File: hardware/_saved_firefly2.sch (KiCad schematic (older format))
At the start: 20 parts, among them J1 10118194-0001LF, P2 CONN_01X03, P3 CONN_01X04, P4 CONN_01X05, P5 CONN_01X01, U1 SAM_D11C, U2 RFM69CW, U3 MIC5504

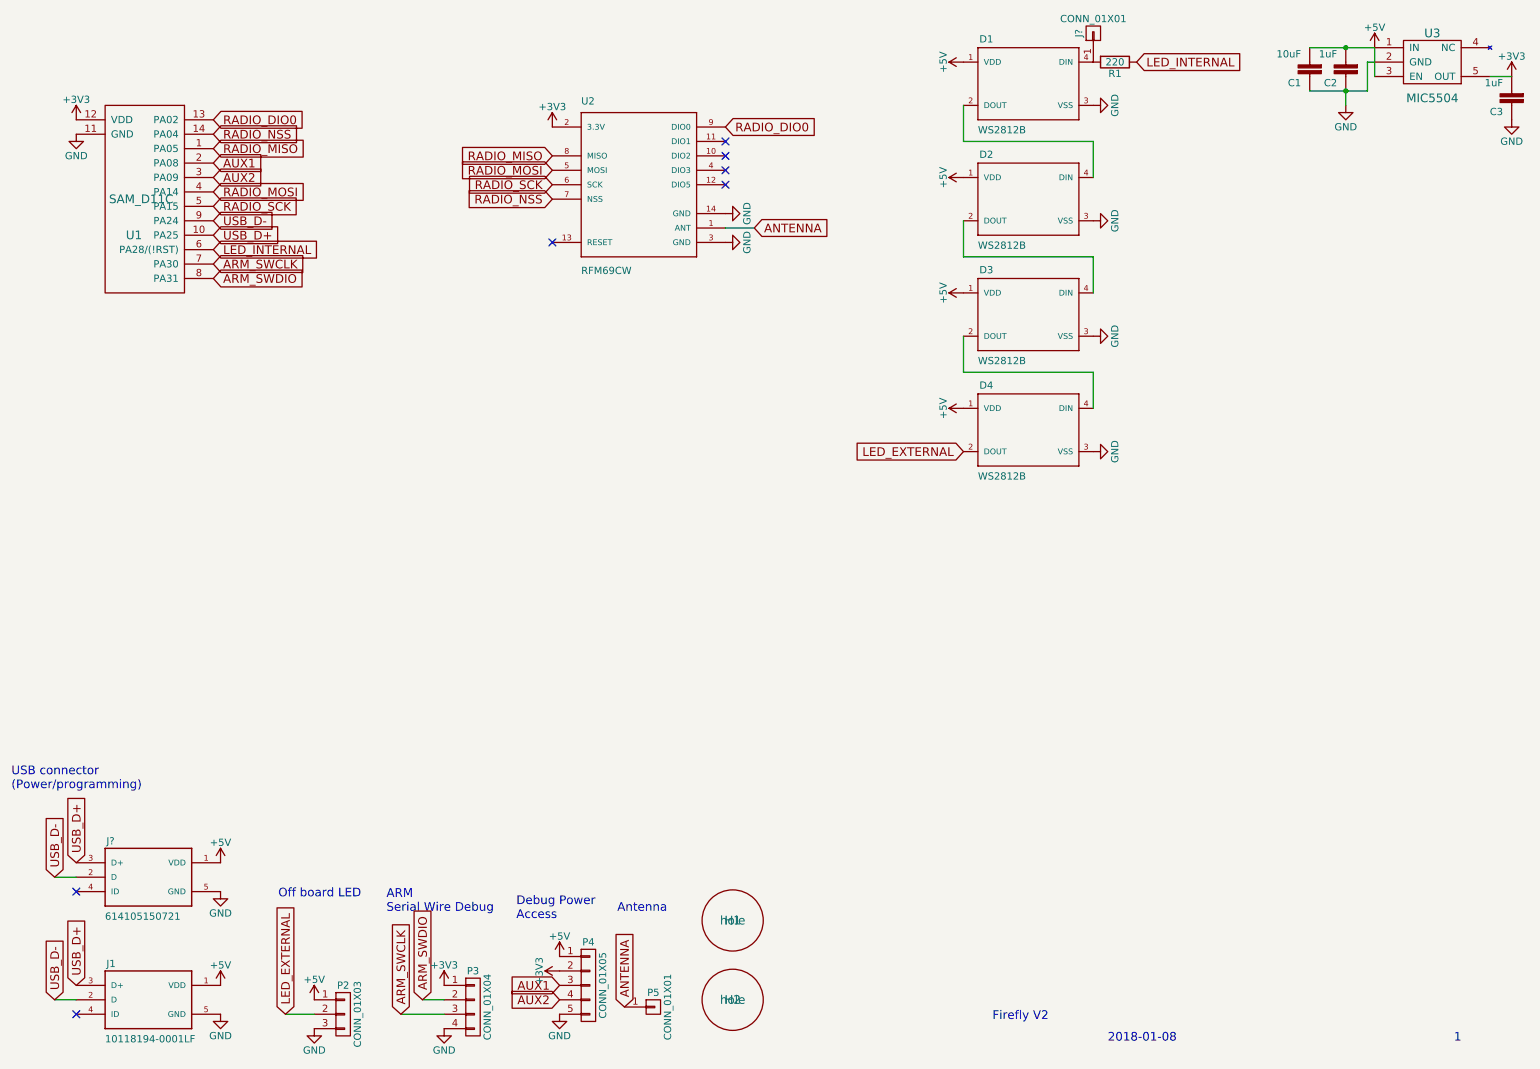
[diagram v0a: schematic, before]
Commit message: Hardware v2.1 Mark orientation for LEDs and radio. Tie enable high on the LDO. Add vertical USB connector and fix horizontal USB connector.
Change-Id: I3b6b9a9fcd473732bc67a64c80cbd03d1b6050b8
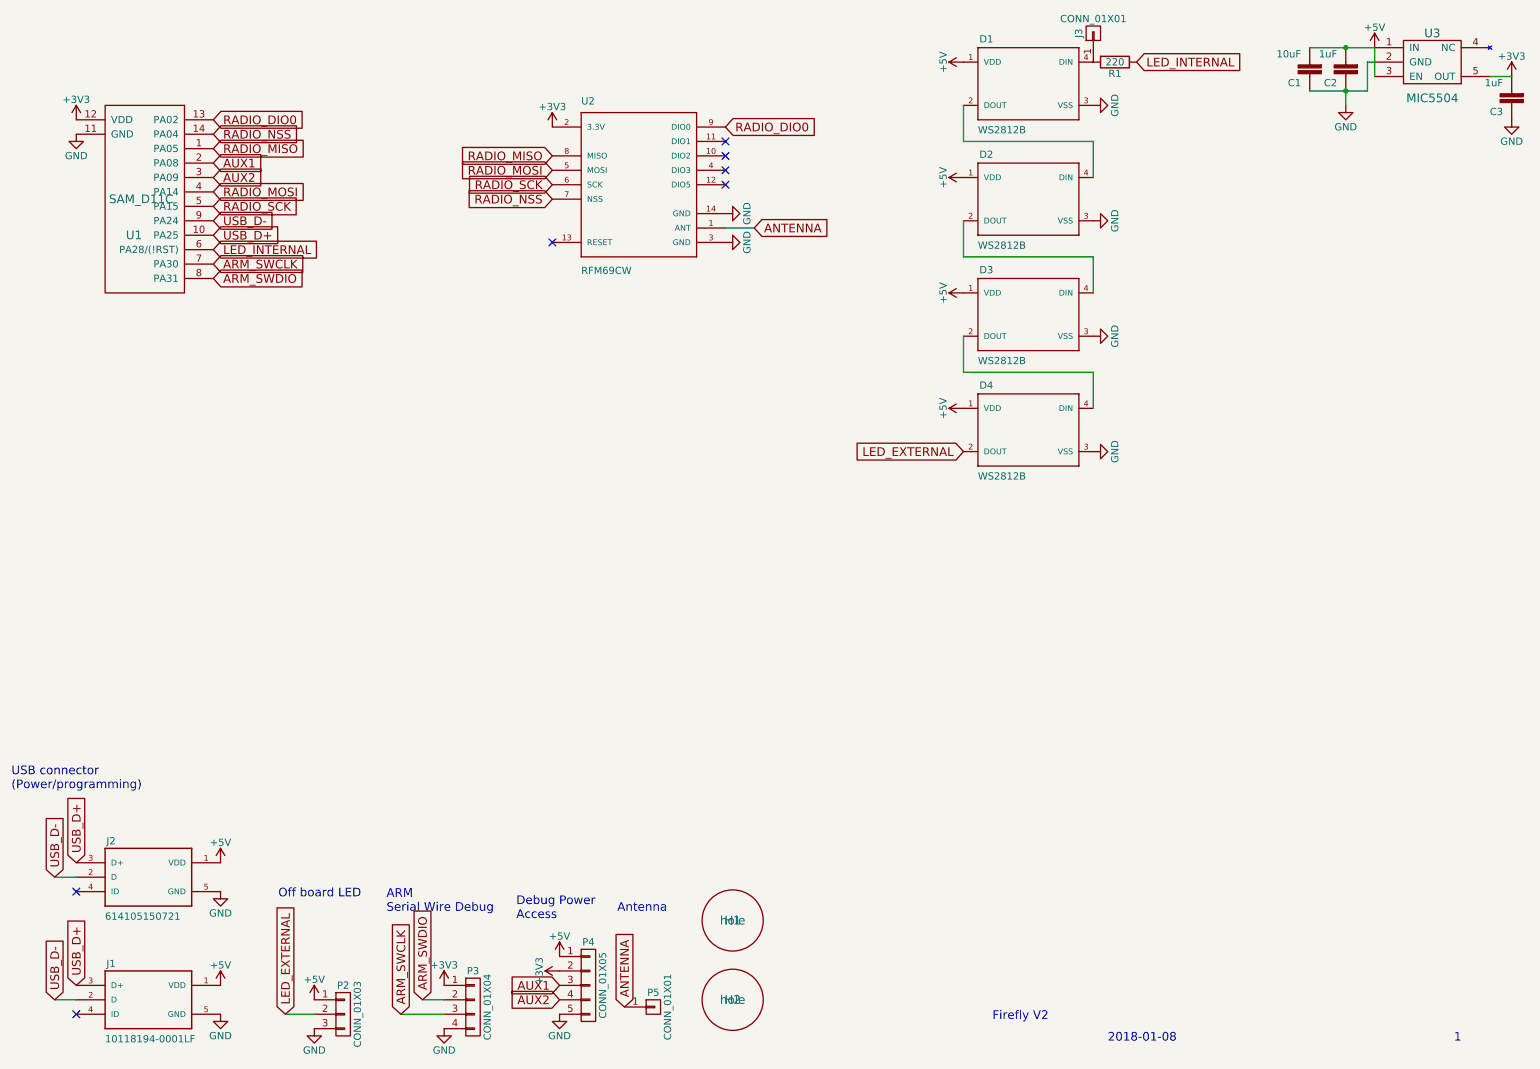
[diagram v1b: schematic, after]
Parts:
- J2: renamed from J?; footprint 10118194-0001LF:FRAMATOME_10118194-0001LF -> Connector_USB:USB_Micro-B_Wuerth-614105150721_Vertical
- J3: renamed from J?; footprint (none) -> Pin_Headers:Pin_Header_Straight_1x01_Pitch1.27mm
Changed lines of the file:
@@
 	10000 750  10000 950
 $Comp
-L CONN_01X01 J?
+L CONN_01X01 J3
 U 1 1 5A6CACDA
 P 8050 650
-F 0 "J?" H 8050 750 50  0000 C CNN
+F 0 "J3" H 8050 750 50  0000 C CNN
 F 1 "CONN_01X01" V 8150 650 50  0000 C CNN
-F 2 "" H 8050 650 50  0001 C CNN
+F 2 "Pin_Headers:Pin_Header_Straight_1x01_Pitch1.27mm" H 8050 650 50  0001 C CNN
 F 3 "" H 8050 650 50  0001 C CNN
 	1    8050 650
@@
 USB connector\n(Power/programming)
 $Comp
-L +5V #PWR?
+L +5V #PWR027
 U 1 1 5A6CC722
 P 2000 6400
-F 0 "#PWR?" H 2000 6250 50  0001 C CNN
+F 0 "#PWR027" H 2000 6250 50  0001 C CNN
 F 1 "+5V" H 2000 6540 50  0000 C CNN
 F 2 "" H 2000 6400 50  0000 C CNN
@@
 $EndComp
 $Comp
-L GND #PWR?
+L GND #PWR028
 U 1 1 5A6CC728
 P 2000 6600
-F 0 "#PWR?" H 2000 6350 50  0001 C CNN
+F 0 "#PWR028" H 2000 6350 50  0001 C CNN
 F 1 "GND" H 2000 6450 50  0000 C CNN
 F 2 "" H 2000 6600 50  0000 C CNN
@@
 	850  6500 1000 6500
 $Comp
-L 10118194-0001LF J?
+L 10118194-0001LF J2
 U 1 1 5A6CC736
 P 1500 6500
-F 0 "J?" H 1209 6721 50  0000 L BNN
+F 0 "J2" H 1209 6721 50  0000 L BNN
 F 1 "614105150721" H 1199 6199 50  0000 L BNN
-F 2 "10118194-0001LF:FRAMATOME_10118194-0001LF" H 1500 6500 50  0001 L BNN
+F 2 "Connector_USB:USB_Micro-B_Wuerth-614105150721_Vertical" H 1500 6500 50  0001 L BNN
 F 3 "Amphenol" H 1500 6500 50  0001 L BNN
 F 4 "0.25 USD" H 1500 6500 50  0001 L BNN "Field4"
